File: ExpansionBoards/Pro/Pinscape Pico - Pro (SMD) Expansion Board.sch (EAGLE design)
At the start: 209 parts, among them IC1 UCC27523D, IC10 UCC27523D, IC11 UCC27523D, IC12 UCC27523D, IC13 UCC27523D, IC14 UCC27523D, IC15 TLC59116FIRHBR, IC16 TLC59116FIRHBR, IC17 TLC59116FIRHBR, IC18 TLC59116FIRHBR, IC19 ULN2803ADWR, IC2 UCC27523D, IC20 ULN2803ADWR, IC21 ULN2803ADWR, IC22 ULN2803ADWR, IC23 ULN2803ADWR, IC24 SN74HC165PWR, IC25 SN74HC165PWR, IC26 SN74HC165PWR, IC27 SN74HC165PWR, IC28 LIS3DHTR, IC29 SN74LVC1G175DCKR, IC3 UCC27523D, IC30 APX809S-29SA-7, IC31 LTV-827S, IC32 ADS1115IDGSR, IC33 TLV75733PDBVR, IC34 RV-3032-C7, IC4 UCC27523D, IC5 UCC27523D, IC6 UCC27523D, IC7 UCC27523D, IC8 UCC27523D, IC9 UCC27523D, J1 640445-6, J10 1-640456-0, J11 1-640456-0, J12 1-640456-0, J13 640445-5, J14 640445-9, J15 640445-9, J16 640445-9, J2 30316-6002HB, J3 1-640456-0, J4 640456-9, J5 640456-9, J6 640454-2, J7 215079-4, J8 30308-6002HB, J9 1-640456-0, Q1 BUK7K89-100EX, Q10 BUK7K89-100EX, Q11 BUK7K89-100EX, Q12 BUK7K89-100EX, Q13 BUK7K89-100EX, Q14 BUK7K89-100EX, Q15 UMA5NTR, Q16 UMA5NTR, Q17 UMA5NTR, Q18 UMA5NTR, Q19 UMA5NTR, Q2 BUK7K89-100EX, Q20 UMA5NTR, Q21 UMA5NTR, Q22 UMA5NTR, Q23 UMA5NTR, Q24 UMA5NTR, Q25 UMA5NTR, Q26 UMA5NTR, Q27 DSS8110Y-7, Q3 BUK7K89-100EX, Q4 BUK7K89-100EX, Q5 BUK7K89-100EX, Q6 BUK7K89-100EX, Q7 BUK7K89-100EX, Q8 BUK7K89-100EX, Q9 BUK7K89-100EX, SW1 TS-1187A-B-A-B, U1 BAT-HLD-001-THM

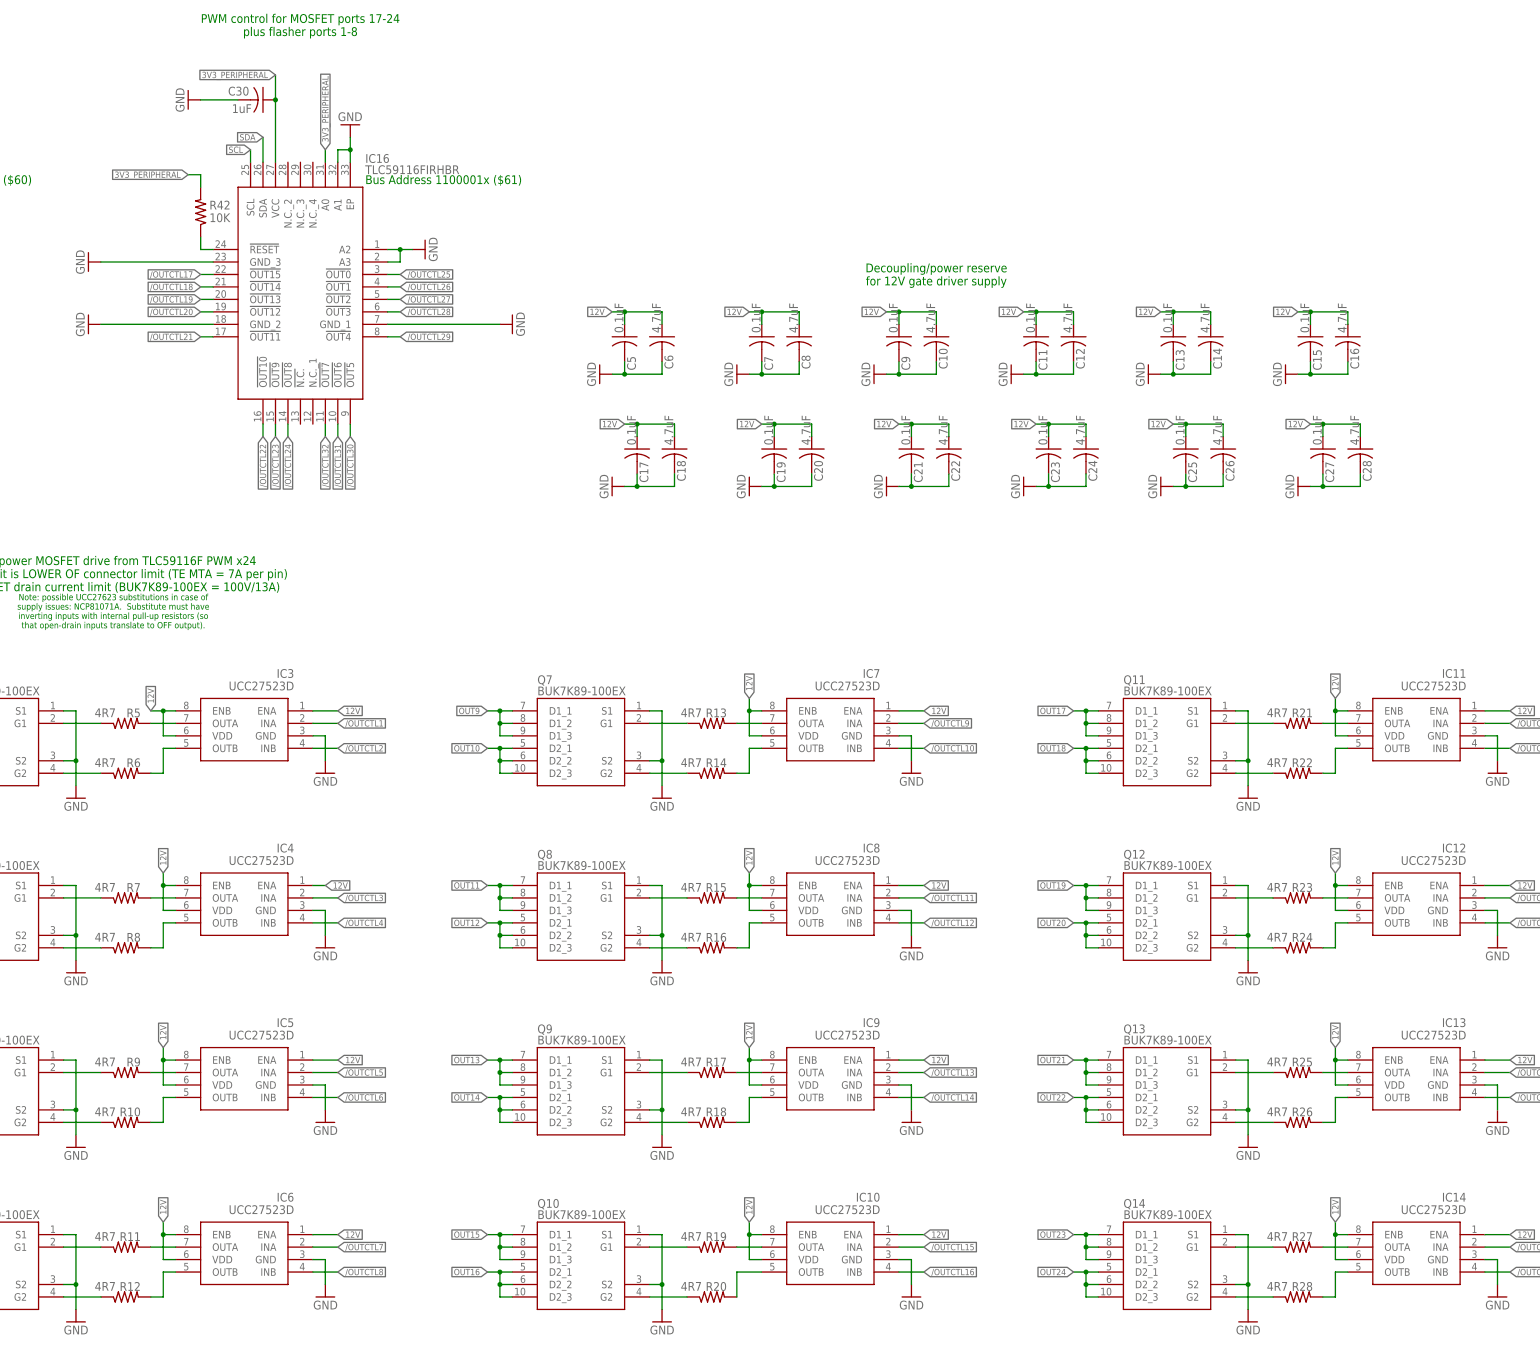
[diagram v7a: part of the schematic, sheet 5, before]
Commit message: Exp boards: update gate resistors in BOMs
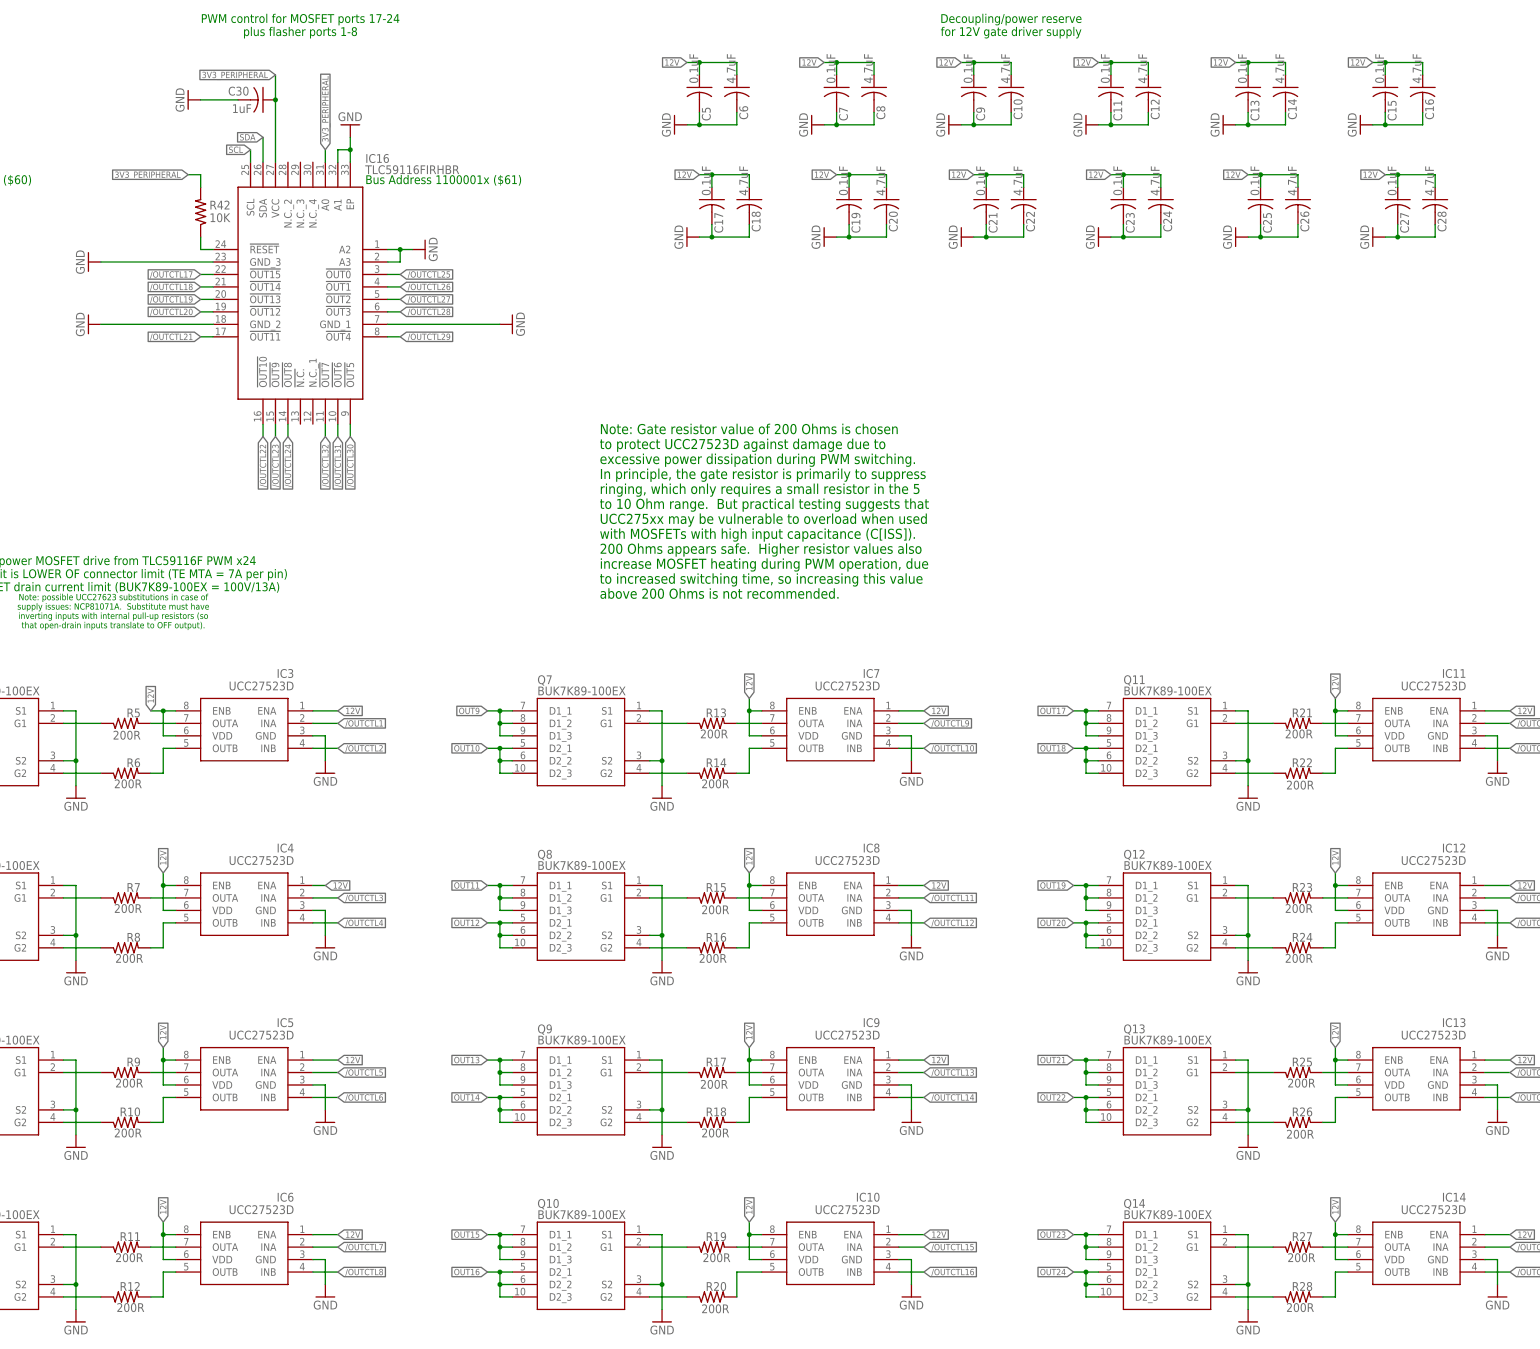
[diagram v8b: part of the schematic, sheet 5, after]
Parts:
- R10, R11, R12, R13, R14, R15, R16, R17, R18, R19, R20, R21, R22, R23, R24, R25, R26, R27, R28, R5, R6, R7, R8, R9: value 4R7 -> 200R
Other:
- note added: "Note: Gate resistor value of 200 Ohms is chosen to protect UCC27523D against damage due to excessive power dissipation during PWM switching. In principle, the gate resistor is primarily to suppress ringing, which only requires a small resistor in the 5 to 10 Ohm range. But practical testing suggests that UCC275xx may be vulnerable to overload when used with MOSFETs with high input capacitance (C[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"
- moved on the sheet: C10, C11, C12, C13, C14, C15, C16, C17, C18, C19, C20, C21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
